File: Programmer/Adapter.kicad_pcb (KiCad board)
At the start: 2 copper layers, 38.1 x 20.3 mm, 5 parts, among them IC1 ARDUINO_PRO_MINI_BASIC, P1 CONN_01X06, P2 CONN_01X02, SW1 SWITCH_SPDT, SW2 SWITCH_SPDT

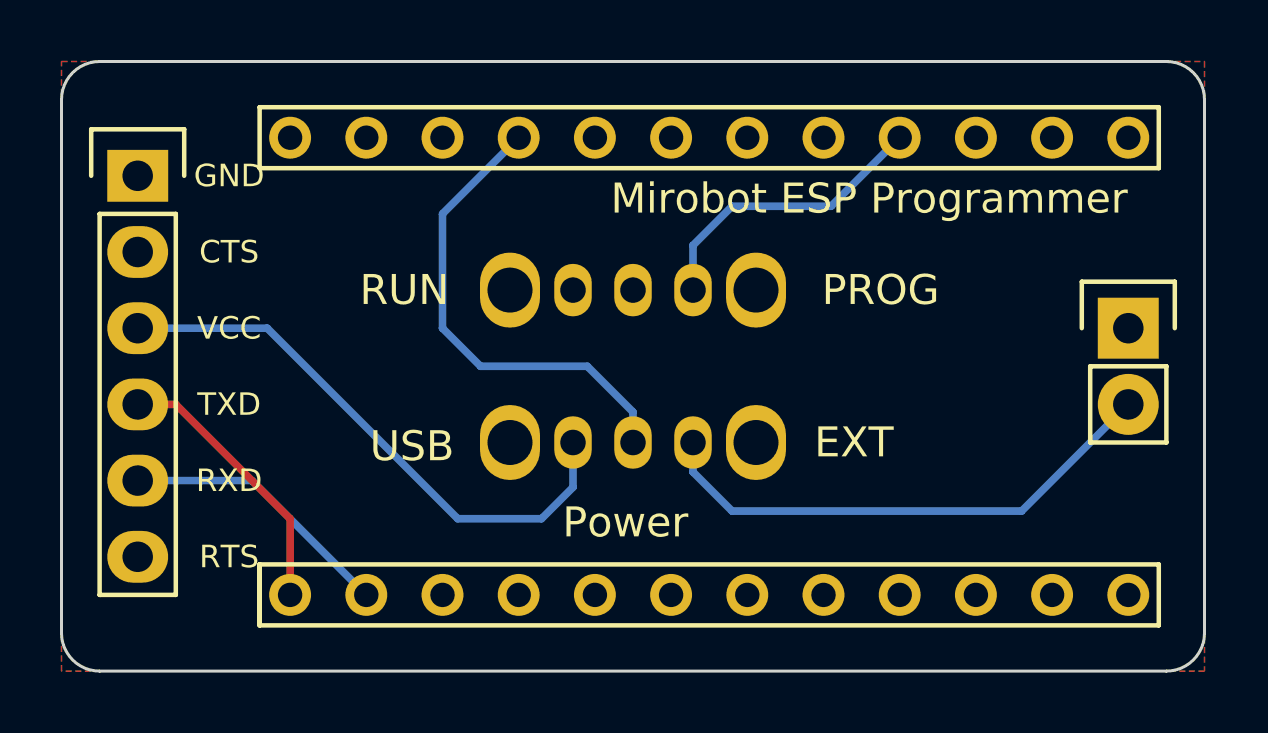
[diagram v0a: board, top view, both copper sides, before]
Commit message: Use a different pin for bringing GPIO0 out
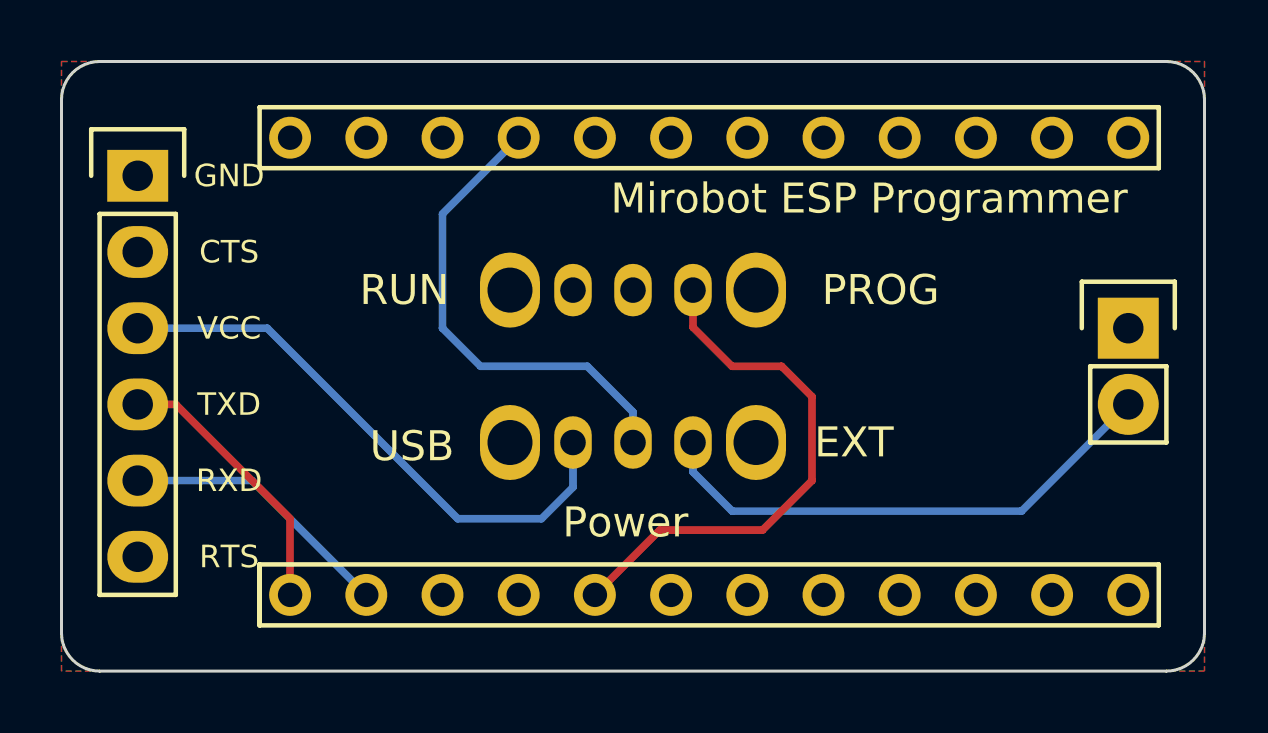
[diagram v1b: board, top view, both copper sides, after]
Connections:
- IC1 pad 16: Net-(IC1-Pad16) -> (no net)
- IC1 pad 5: (no net) -> Net-(IC1-Pad5)
- SW2 pad 1: Net-(IC1-Pad16) -> Net-(IC1-Pad5)
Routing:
- net Net-(IC1-Pad5): track 0.00 -> 17.8 mm
- net Net-(IC1-Pad16): track 9.87 -> 0.00 mm
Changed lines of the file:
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@@
     (thickness 1.6)
     (drawings 20)
-    (tracks 24)
+    (tracks 28)
     (zones 0)
     (modules 5)
@@
   (net 4 GND)
   (net 5 "Net-(P1-Pad3)")
-  (net 6 "Net-(IC1-Pad16)")
-  (net 7 "Net-(P2-Pad2)")
+  (net 6 "Net-(P2-Pad2)")
+  (net 7 "Net-(IC1-Pad5)")
   (net_class Default "This is the default net class."
     (clearance 0.254)
@@
     (add_net GND)
     (add_net "Net-(IC1-Pad1)")
-    (add_net "Net-(IC1-Pad16)")
     (add_net "Net-(IC1-Pad2)")
     (add_net "Net-(IC1-Pad21)")
+    (add_net "Net-(IC1-Pad5)")
     (add_net "Net-(P1-Pad3)")
     (add_net "Net-(P2-Pad2)")
@@
       (net 4 GND))
     (pad 2 thru_hole oval (at 0 2.54) (size 2.032 2.032) (drill 1.016) (layers *.Cu *.Mask F.SilkS)
-      (net 7 "Net-(P2-Pad2)"))
+      (net 6 "Net-(P2-Pad2)"))
     (model Pin_Headers.3dshapes/Pin_Header_Straight_1x02.wrl
       (at (xyz 0 -0.05 0))
@@
     (pad 4 thru_hole circle (at -6.35 7.62) (size 1.397 1.397) (drill 0.8128) (layers *.Cu *.Mask F.SilkS)
       (net 4 GND))
-    (pad 5 thru_hole circle (at -3.81 7.62) (size 1.397 1.397) (drill 0.8128) (layers *.Cu *.Mask F.SilkS))
+    (pad 5 thru_hole circle (at -3.81 7.62) (size 1.397 1.397) (drill 0.8128) (layers *.Cu *.Mask F.SilkS)
+      (net 7 "Net-(IC1-Pad5)"))
     (pad 6 thru_hole circle (at -1.27 7.62) (size 1.397 1.397) (drill 0.8128) (layers *.Cu *.Mask F.SilkS))
     (pad 7 thru_hole circle (at 1.27 7.62) (size 1.397 1.397) (drill 0.8128) (layers *.Cu *.Mask F.SilkS))
@@
     (pad 14 thru_hole circle (at 11.43 -7.62) (size 1.397 1.397) (drill 0.8128) (layers *.Cu *.Mask F.SilkS))
     (pad 15 thru_hole circle (at 8.89 -7.62) (size 1.397 1.397) (drill 0.8128) (layers *.Cu *.Mask F.SilkS))
-    (pad 16 thru_hole circle (at 6.35 -7.62) (size 1.397 1.397) (drill 0.8128) (layers *.Cu *.Mask F.SilkS)
-      (net 6 "Net-(IC1-Pad16)"))
+    (pad 16 thru_hole circle (at 6.35 -7.62) (size 1.397 1.397) (drill 0.8128) (layers *.Cu *.Mask F.SilkS))
     (pad 17 thru_hole circle (at 3.81 -7.62) (size 1.397 1.397) (drill 0.8128) (layers *.Cu *.Mask F.SilkS))
     (pad 18 thru_hole circle (at 1.27 -7.62) (size 1.397 1.397) (drill 0.8128) (layers *.Cu *.Mask F.SilkS))
@@
       (net 5 "Net-(P1-Pad3)"))
     (pad 3 thru_hole oval (at -2 0 180) (size 1.25 1.75) (drill 0.85) (layers *.Cu *.Mask F.SilkS)
-      (net 7 "Net-(P2-Pad2)"))
+      (net 6 "Net-(P2-Pad2)"))
     (pad 4 thru_hole oval (at 4.1 0 180) (size 2 2.5) (drill 1.5) (layers *.Cu *.Mask F.SilkS))
     (pad 5 thru_hole oval (at -4.1 0 180) (size 2 2.5) (drill 1.5) (layers *.Cu *.Mask F.SilkS))
@@
       (net 4 GND))
     (pad 1 thru_hole oval (at 2 0) (size 1.25 1.75) (drill 0.85) (layers *.Cu *.Mask F.SilkS)
-      (net 6 "Net-(IC1-Pad16)"))
+      (net 7 "Net-(IC1-Pad5)"))
     (pad 3 thru_hole oval (at -2 0) (size 1.25 1.75) (drill 0.85) (layers *.Cu *.Mask F.SilkS))
     (pad 4 thru_hole oval (at 4.1 0) (size 2 2.5) (drill 1.5) (layers *.Cu *.Mask F.SilkS))
@@
   (gr_line (start 165.1 93.98) (end 129.54 93.98) (angle 90) (layer Edge.Cuts) (width 0.1))
   (gr_line (start 166.37 113.03) (end 166.37 95.25) (angle 90) (layer Edge.Cuts) (width 0.1))
+  (segment (start 130.81 105.41) (end 132.08 105.41) (width 0.254) (layer F.Cu) (net 1) (status 10))
+  (segment (start 135.89 109.22) (end 135.89 111.76) (width 0.254) (layer F.Cu) (net 1) (status 20))
   (segment (start 132.08 105.41) (end 135.89 109.22) (width 0.254) (layer F.Cu) (net 1))
-  (segment (start 135.89 109.22) (end 135.89 111.76) (width 0.254) (layer F.Cu) (net 1) (status 20))
-  (segment (start 130.81 105.41) (end 132.08 105.41) (width 0.254) (layer F.Cu) (net 1) (status 10))
+  (segment (start 130.81 107.95) (end 134.62 107.95) (width 0.254) (layer B.Cu) (net 2) (status 10))
   (segment (start 134.62 107.95) (end 138.43 111.76) (width 0.254) (layer B.Cu) (net 2) (status 20))
-  (segment (start 130.81 107.95) (end 134.62 107.95) (width 0.254) (layer B.Cu) (net 2) (status 10))
+  (segment (start 147.32 106.68) (end 147.32 105.664) (width 0.254) (layer B.Cu) (net 3))
+  (segment (start 140.97 99.06) (end 143.51 96.52) (width 0.254) (layer B.Cu) (net 3))
+  (segment (start 140.97 102.87) (end 140.97 99.06) (width 0.254) (layer B.Cu) (net 3))
+  (segment (start 142.24 104.14) (end 140.97 102.87) (width 0.254) (layer B.Cu) (net 3))
+  (segment (start 145.796 104.14) (end 142.24 104.14) (width 0.254) (layer B.Cu) (net 3))
   (segment (start 147.32 105.664) (end 145.796 104.14) (width 0.254) (layer B.Cu) (net 3))
-  (segment (start 145.796 104.14) (end 142.24 104.14) (width 0.254) (layer B.Cu) (net 3))
-  (segment (start 142.24 104.14) (end 140.97 102.87) (width 0.254) (layer B.Cu) (net 3))
-  (segment (start 140.97 102.87) (end 140.97 99.06) (width 0.254) (layer B.Cu) (net 3))
-  (segment (start 140.97 99.06) (end 143.51 96.52) (width 0.254) (layer B.Cu) (net 3))
-  (segment (start 147.32 106.68) (end 147.32 105.664) (width 0.254) (layer B.Cu) (net 3))
+  (segment (start 130.81 102.87) (end 135.128 102.87) (width 0.254) (layer B.Cu) (net 5))
+  (segment (start 145.32 108.172) (end 145.32 106.68) (width 0.254) (layer B.Cu) (net 5))
+  (segment (start 144.272 109.22) (end 145.32 108.172) (width 0.254) (layer B.Cu) (net 5))
+  (segment (start 141.478 109.22) (end 144.272 109.22) (width 0.254) (layer B.Cu) (net 5))
   (segment (start 135.128 102.87) (end 141.478 109.22) (width 0.254) (layer B.Cu) (net 5))
-  (segment (start 141.478 109.22) (end 144.272 109.22) (width 0.254) (layer B.Cu) (net 5))
-  (segment (start 144.272 109.22) (end 145.32 108.172) (width 0.254) (layer B.Cu) (net 5))
-  (segment (start 145.32 108.172) (end 145.32 106.68) (width 0.254) (layer B.Cu) (net 5))
-  (segment (start 130.81 102.87) (end 135.128 102.87) (width 0.254) (layer B.Cu) (net 5))
-  (segment (start 153.924 98.806) (end 150.622 98.806) (width 0.254) (layer B.Cu) (net 6))
-  (segment (start 150.622 98.806) (end 149.32 100.108) (width 0.254) (layer B.Cu) (net 6))
-  (segment (start 149.32 100.108) (end 149.32 101.6) (width 0.254) (layer B.Cu) (net 6))
-  (segment (start 156.21 96.52) (end 153.924 98.806) (width 0.254) (layer B.Cu) (net 6))
-  (segment (start 149.32 107.664) (end 150.622 108.966) (width 0.254) (layer B.Cu) (net 7))
-  (segment (start 150.622 108.966) (end 160.274 108.966) (width 0.254) (layer B.Cu) (net 7))
-  (segment (start 160.274 108.966) (end 163.83 105.41) (width 0.254) (layer B.Cu) (net 7))
-  (segment (start 149.32 106.68) (end 149.32 107.664) (width 0.254) (layer B.Cu) (net 7))
+  (segment (start 149.32 106.68) (end 149.32 107.664) (width 0.254) (layer B.Cu) (net 6))
+  (segment (start 160.274 108.966) (end 163.83 105.41) (width 0.254) (layer B.Cu) (net 6))
+  (segment (start 150.622 108.966) (end 160.274 108.966) (width 0.254) (layer B.Cu) (net 6))
+  (segment (start 149.32 107.664) (end 150.622 108.966) (width 0.254) (layer B.Cu) (net 6))
+  (segment (start 149.32 101.6) (end 149.32 102.838) (width 0.254) (layer F.Cu) (net 7))
+  (segment (start 148.209 109.601) (end 146.05 111.76) (width 0.254) (layer F.Cu) (net 7))
+  (segment (start 151.638 109.601) (end 148.209 109.601) (width 0.254) (layer F.Cu) (net 7))
+  (segment (start 153.289 107.95) (end 151.638 109.601) (width 0.254) (layer F.Cu) (net 7))
+  (segment (start 153.289 105.156) (end 153.289 107.95) (width 0.254) (layer F.Cu) (net 7))
+  (segment (start 152.273 104.14) (end 153.289 105.156) (width 0.254) (layer F.Cu) (net 7))
+  (segment (start 150.622 104.14) (end 152.273 104.14) (width 0.254) (layer F.Cu) (net 7))
+  (segment (start 149.32 102.838) (end 150.622 104.14) (width 0.254) (layer F.Cu) (net 7))
   (zone (net 4) (net_name GND) (layer F.Cu) (hatch edge 0.508)
     (connect_pads (clearance 0.508))

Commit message: Final production release for v2
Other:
- board text added: "+"
- board text added: "-"
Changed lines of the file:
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@@
     (links 10)
     (no_connects 0)
-    (area 128.219999 93.929999 166.420001 114.350001)
+    (area 125.647667 91.511 168.992334 114.350001)
     (thickness 1.6)
-    (drawings 20)
+    (drawings 24)
     (tracks 28)
     (zones 0)
@@
     (pad 5 thru_hole oval (at -4.1 0) (size 2 2.5) (drill 1.5) (layers *.Cu *.Mask F.SilkS))
   )
+  (dimension 20.32 (width 0.3) (layer Eco1.User)
+    (gr_text "20.320 mm" (at 170.768 104.14 270) (layer Eco1.User)
+      (effects (font (size 1.5 1.5) (thickness 0.3)))
+    )
+    (feature1 (pts (xy 167.132 114.3) (xy 172.118 114.3)))
+    (feature2 (pts (xy 167.132 93.98) (xy 172.118 93.98)))
+    (crossbar (pts (xy 169.418 93.98) (xy 169.418 114.3)))
+    (arrow1a (pts (xy 169.418 114.3) (xy 168.831579 113.173496)))
+    (arrow1b (pts (xy 169.418 114.3) (xy 170.004421 113.173496)))
+    (arrow2a (pts (xy 169.418 93.98) (xy 168.831579 95.106504)))
+    (arrow2b (pts (xy 169.418 93.98) (xy 170.004421 95.106504)))
+  )
+  (dimension 38.1 (width 0.3) (layer Eco1.User)
+    (gr_text "38.100 mm" (at 147.32 90.598) (layer Eco1.User)
+      (effects (font (size 1.5 1.5) (thickness 0.3)))
+    )
+    (feature1 (pts (xy 128.27 93.218) (xy 128.27 89.248)))
+    (feature2 (pts (xy 166.37 93.218) (xy 166.37 89.248)))
+    (crossbar (pts (xy 166.37 91.948) (xy 128.27 91.948)))
+    (arrow1a (pts (xy 128.27 91.948) (xy 129.396504 91.361579)))
+    (arrow1b (pts (xy 128.27 91.948) (xy 129.396504 92.534421)))
+    (arrow2a (pts (xy 166.37 91.948) (xy 165.243496 91.361579)))
+    (arrow2b (pts (xy 166.37 91.948) (xy 165.243496 92.534421)))
+  )
+  (gr_text - (at 163.83 99.822) (layer F.SilkS)
+    (effects (font (size 1.5 1.5) (thickness 0.375)) (justify mirror))
+  )
+  (gr_text + (at 163.83 108.204) (layer F.SilkS)
+    (effects (font (size 1.5 1.5) (thickness 0.375)) (justify mirror))
+  )
   (gr_text Power (at 147.066 109.347) (layer F.SilkS)
     (effects (font (size 1 1) (thickness 0.15)))
@@
   (gr_line (start 165.1 93.98) (end 129.54 93.98) (angle 90) (layer Edge.Cuts) (width 0.1))
   (gr_line (start 166.37 113.03) (end 166.37 95.25) (angle 90) (layer Edge.Cuts) (width 0.1))
+  (segment (start 132.08 105.41) (end 135.89 109.22) (width 0.254) (layer F.Cu) (net 1))
+  (segment (start 135.89 109.22) (end 135.89 111.76) (width 0.254) (layer F.Cu) (net 1) (status 20))
   (segment (start 130.81 105.41) (end 132.08 105.41) (width 0.254) (layer F.Cu) (net 1) (status 10))
-  (segment (start 135.89 109.22) (end 135.89 111.76) (width 0.254) (layer F.Cu) (net 1) (status 20))
-  (segment (start 132.08 105.41) (end 135.89 109.22) (width 0.254) (layer F.Cu) (net 1))
+  (segment (start 134.62 107.95) (end 138.43 111.76) (width 0.254) (layer B.Cu) (net 2) (status 20))
   (segment (start 130.81 107.95) (end 134.62 107.95) (width 0.254) (layer B.Cu) (net 2) (status 10))
-  (segment (start 134.62 107.95) (end 138.43 111.76) (width 0.254) (layer B.Cu) (net 2) (status 20))
+  (segment (start 147.32 105.664) (end 145.796 104.14) (width 0.254) (layer B.Cu) (net 3))
+  (segment (start 145.796 104.14) (end 142.24 104.14) (width 0.254) (layer B.Cu) (net 3))
+  (segment (start 142.24 104.14) (end 140.97 102.87) (width 0.254) (layer B.Cu) (net 3))
+  (segment (start 140.97 102.87) (end 140.97 99.06) (width 0.254) (layer B.Cu) (net 3))
+  (segment (start 140.97 99.06) (end 143.51 96.52) (width 0.254) (layer B.Cu) (net 3))
   (segment (start 147.32 106.68) (end 147.32 105.664) (width 0.254) (layer B.Cu) (net 3))
-  (segment (start 140.97 99.06) (end 143.51 96.52) (width 0.254) (layer B.Cu) (net 3))
-  (segment (start 140.97 102.87) (end 140.97 99.06) (width 0.254) (layer B.Cu) (net 3))
-  (segment (start 142.24 104.14) (end 140.97 102.87) (width 0.254) (layer B.Cu) (net 3))
-  (segment (start 145.796 104.14) (end 142.24 104.14) (width 0.254) (layer B.Cu) (net 3))
-  (segment (start 147.32 105.664) (end 145.796 104.14) (width 0.254) (layer B.Cu) (net 3))
+  (segment (start 135.128 102.87) (end 141.478 109.22) (width 0.254) (layer B.Cu) (net 5))
+  (segment (start 141.478 109.22) (end 144.272 109.22) (width 0.254) (layer B.Cu) (net 5))
+  (segment (start 144.272 109.22) (end 145.32 108.172) (width 0.254) (layer B.Cu) (net 5))
+  (segment (start 145.32 108.172) (end 145.32 106.68) (width 0.254) (layer B.Cu) (net 5))
   (segment (start 130.81 102.87) (end 135.128 102.87) (width 0.254) (layer B.Cu) (net 5))
-  (segment (start 145.32 108.172) (end 145.32 106.68) (width 0.254) (layer B.Cu) (net 5))
-  (segment (start 144.272 109.22) (end 145.32 108.172) (width 0.254) (layer B.Cu) (net 5))
-  (segment (start 141.478 109.22) (end 144.272 109.22) (width 0.254) (layer B.Cu) (net 5))
-  (segment (start 135.128 102.87) (end 141.478 109.22) (width 0.254) (layer B.Cu) (net 5))
+  (segment (start 149.32 107.664) (end 150.622 108.966) (width 0.254) (layer B.Cu) (net 6))
+  (segment (start 150.622 108.966) (end 160.274 108.966) (width 0.254) (layer B.Cu) (net 6))
+  (segment (start 160.274 108.966) (end 163.83 105.41) (width 0.254) (layer B.Cu) (net 6))
   (segment (start 149.32 106.68) (end 149.32 107.664) (width 0.254) (layer B.Cu) (net 6))
-  (segment (start 160.274 108.966) (end 163.83 105.41) (width 0.254) (layer B.Cu) (net 6))
-  (segment (start 150.622 108.966) (end 160.274 108.966) (width 0.254) (layer B.Cu) (net 6))
-  (segment (start 149.32 107.664) (end 150.622 108.966) (width 0.254) (layer B.Cu) (net 6))
+  (segment (start 149.32 102.838) (end 150.622 104.14) (width 0.254) (layer F.Cu) (net 7))
+  (segment (start 150.622 104.14) (end 152.273 104.14) (width 0.254) (layer F.Cu) (net 7))
+  (segment (start 152.273 104.14) (end 153.289 105.156) (width 0.254) (layer F.Cu) (net 7))
+  (segment (start 153.289 105.156) (end 153.289 107.95) (width 0.254) (layer F.Cu) (net 7))
+  (segment (start 153.289 107.95) (end 151.638 109.601) (width 0.254) (layer F.Cu) (net 7))
+  (segment (start 151.638 109.601) (end 148.209 109.601) (width 0.254) (layer F.Cu) (net 7))
+  (segment (start 148.209 109.601) (end 146.05 111.76) (width 0.254) (layer F.Cu) (net 7))
   (segment (start 149.32 101.6) (end 149.32 102.838) (width 0.254) (layer F.Cu) (net 7))
-  (segment (start 148.209 109.601) (end 146.05 111.76) (width 0.254) (layer F.Cu) (net 7))
-  (segment (start 151.638 109.601) (end 148.209 109.601) (width 0.254) (layer F.Cu) (net 7))
-  (segment (start 153.289 107.95) (end 151.638 109.601) (width 0.254) (layer F.Cu) (net 7))
-  (segment (start 153.289 105.156) (end 153.289 107.95) (width 0.254) (layer F.Cu) (net 7))
-  (segment (start 152.273 104.14) (end 153.289 105.156) (width 0.254) (layer F.Cu) (net 7))
-  (segment (start 150.622 104.14) (end 152.273 104.14) (width 0.254) (layer F.Cu) (net 7))
-  (segment (start 149.32 102.838) (end 150.622 104.14) (width 0.254) (layer F.Cu) (net 7))
   (zone (net 4) (net_name GND) (layer F.Cu) (hatch edge 0.508)
     (connect_pads (clearance 0.508))
